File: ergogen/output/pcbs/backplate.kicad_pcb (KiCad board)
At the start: 2 copper layers, 124.2 x 110.1 mm, 5 parts

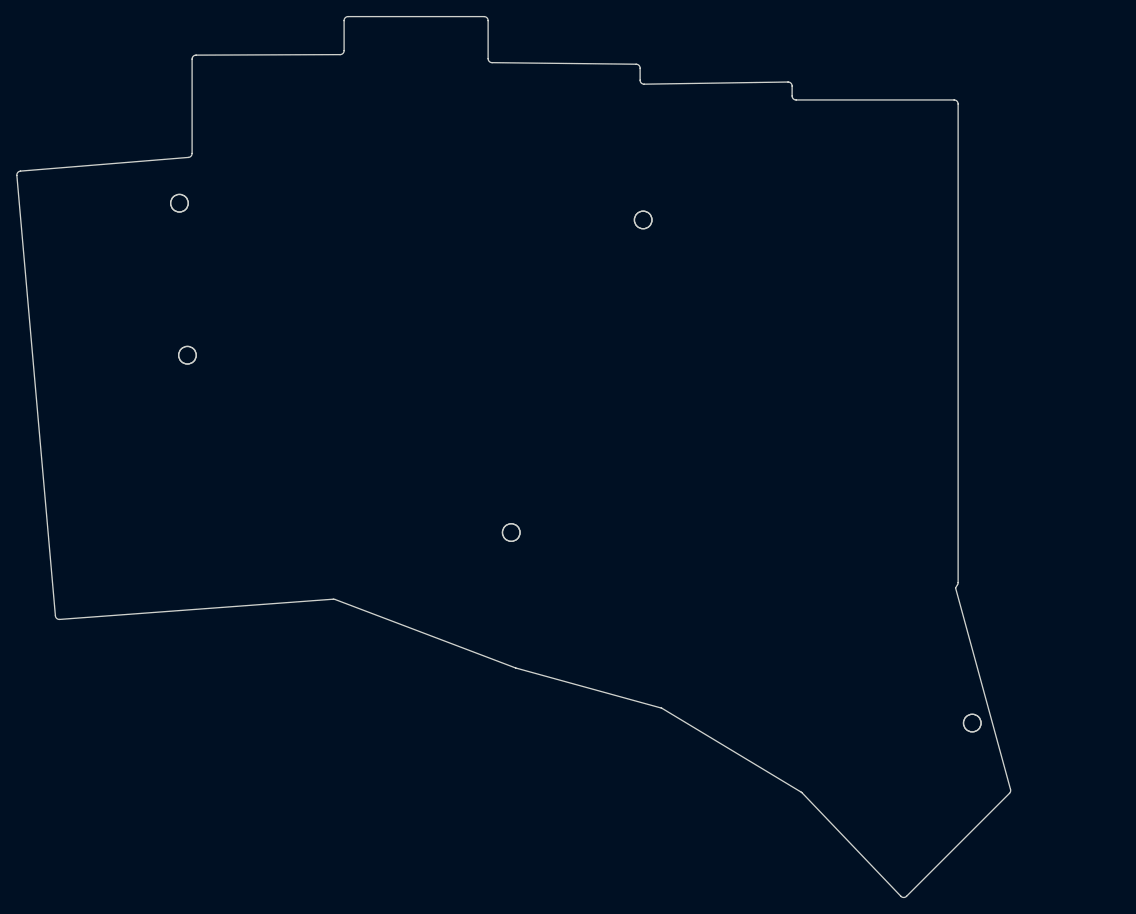
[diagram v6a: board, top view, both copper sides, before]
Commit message: Moved screws around a bit
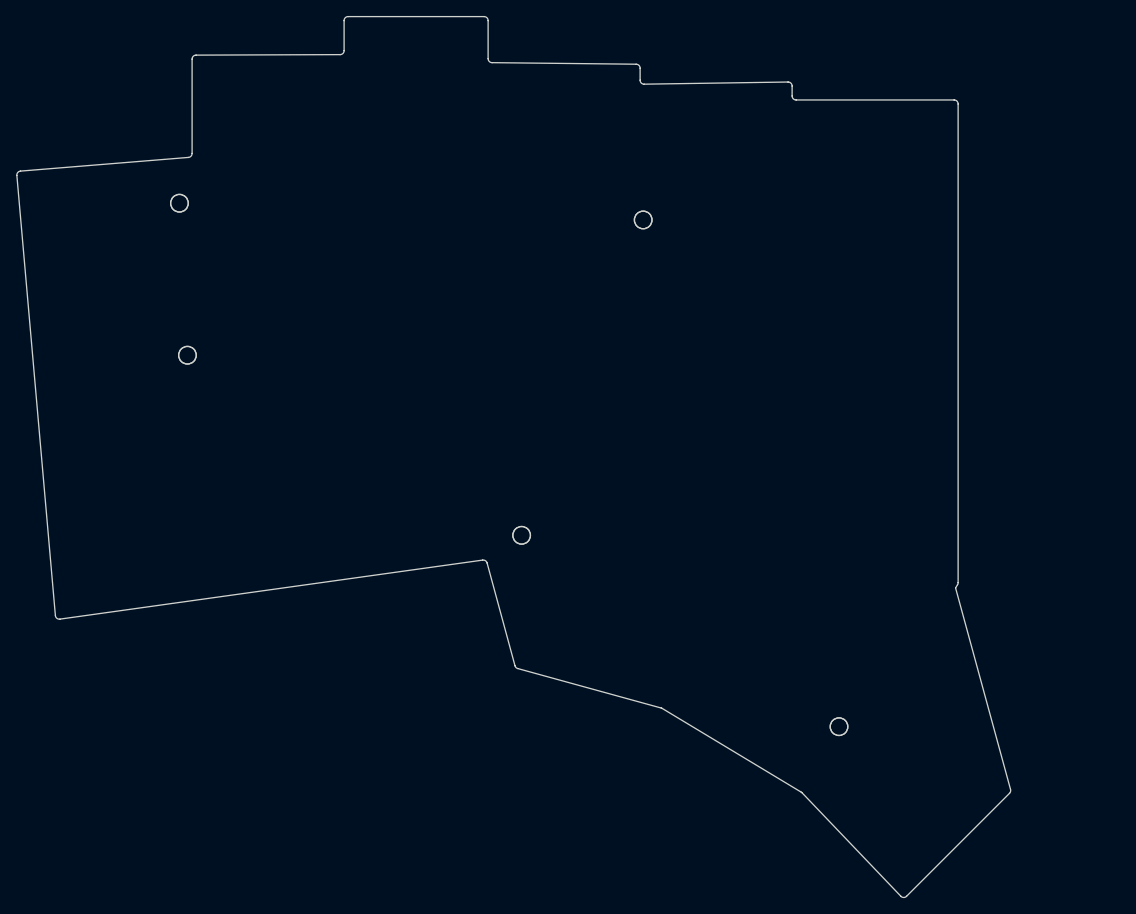
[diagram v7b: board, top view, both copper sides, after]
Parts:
- moved MH5 16.7 mm to (189.8, 123.4), turned to -30 degrees
- moved MH4 1.34 mm to (150.2, 99.4)
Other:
- outline, holes or cut-outs redrawn
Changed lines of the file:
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@@
   )
   (module "ceoloide:mounting_hole_npth" (layer F.Cu)
-      (at 148.8598077 99.0848776 -15)
+      (at 150.1570461 99.4324716 -15)
       (fp_text reference "MH4" (at 0 2.55 -15) (layer F.SilkS) hide (effects (font (size 1 1) (thickness 0.15))))
       (pad "" np_thru_hole circle (at 0 0 -15) (size 2.2 2.2) (drill 2.2) (layers *.Cu *.Mask))
   )
   (module "ceoloide:mounting_hole_npth" (layer F.Cu)
-      (at 206.488576 122.90275019999999 -45)
-      (fp_text reference "MH5" (at 0 2.55 -45) (layer F.SilkS) hide (effects (font (size 1 1) (thickness 0.15))))
-      (pad "" np_thru_hole circle (at 0 0 -45) (size 2.2 2.2) (drill 2.2) (layers *.Cu *.Mask))
+      (at 189.8298246 123.3510864 -30)
+      (fp_text reference "MH5" (at 0 2.55 -30) (layer F.SilkS) hide (effects (font (size 1 1) (thickness 0.15))))
+      (pad "" np_thru_hole circle (at 0 0 -30) (size 2.2 2.2) (drill 2.2) (layers *.Cu *.Mask))
   )
-  (gr_line (start 91.87824460323029 109.49068746980254) (end 87.06061104775414 54.447423555018986) (layer Edge.Cuts) (stroke (width 0.15) (type default)))
+  (gr_line (start 91.87535728883249 109.45769882370212) (end 87.06061104775414 54.447423555018986) (layer Edge.Cuts) (stroke (width 0.15) (type default)))
 (gr_line (start 87.51811429808367 53.90547845906503) (end 108.50503754967045 52.19601094528491) (layer Edge.Cuts) (stroke (width 0.15) (type default)))
 (gr_line (start 108.964445 51.69766144933076) (end 108.964445 39.90788282277217) (layer Edge.Cuts) (stroke (width 0.15) (type default)))
@@
 (gr_line (start 197.5573001306715 144.5456552181502) (end 185.2184018103768 131.6245719172887) (layer Edge.Cuts) (stroke (width 0.15) (type default)))
 (gr_line (start 185.11474537091743 131.54156036435938) (end 167.73632242747522 121.07577102297391) (layer Edge.Cuts) (stroke (width 0.15) (type default)))
-(gr_line (start 167.61101352447525 121.02201021014679) (end 149.42297909295323 116.01776895205687) (layer Edge.Cuts) (stroke (width 0.15) (type default)))
-(gr_line (start 149.37827902664569 116.003177061327) (end 126.82809141312292 107.44890800214452) (layer Edge.Cuts) (stroke (width 0.15) (type default)))
-(gr_line (start 126.61389341312291 107.4177619021445) (end 92.41319770323031 109.94573156980263) (layer Edge.Cuts) (stroke (width 0.15) (type default)))
+(gr_line (start 167.61101352447525 121.02201021014679) (end 149.67542832928424 116.0872276331902) (layer Edge.Cuts) (stroke (width 0.15) (type default)))
+(gr_line (start 149.32552987561743 115.73612318902917) (end 145.83984366392013 102.89472334271511) (layer Edge.Cuts) (stroke (width 0.15) (type default)))
+(gr_line (start 145.28816068340882 102.53050838832783) (end 92.4425969819845 109.90929922465821) (layer Edge.Cuts) (stroke (width 0.15) (type default)))
 (gr_line (start 184.46722317371226 45.01459040000001) (end 204.2174451 45.01459040000001) (layer Edge.Cuts) (stroke (width 0.15) (type default)))
 (gr_line (start 204.7174451 45.51459040000001) (end 204.7174451 105.34161580612954) (layer Edge.Cuts) (stroke (width 0.15) (type default)))
@@
 (gr_arc (start 185.21840173422504 131.62457194226215) (mid 185.16934173422504 131.57960944226215) (end 185.11474533422503 131.54156034226216) (layer Edge.Cuts) (stroke (width 0.15) (type default)))
 (gr_arc (start 167.7363223907828 121.07577100087666) (mid 167.6755091907828 121.04459890087666) (end 167.6110134907828 121.02201020087666) (layer Edge.Cuts) (stroke (width 0.15) (type default)))
-(gr_arc (start 149.37827902664569 116.003177061327) (mid 149.4004574266457 116.010998761327) (end 149.42297912664569 116.017768961327) (layer Edge.Cuts) (stroke (width 0.15) (type default)))
-(gr_arc (start 126.8280914131229 107.4489080021445) (mid 126.72269801312291 107.4216051021445) (end 126.61389341312291 107.4177619021445) (layer Edge.Cuts) (stroke (width 0.15) (type default)))
-(gr_arc (start 91.8782446032303 109.49068746980264) (mid 92.0523782032303 109.82794416980263) (end 92.4131977032303 109.94573156980263) (layer Edge.Cuts) (stroke (width 0.15) (type default)))
+(gr_arc (start 149.32552986297674 115.73612314246033) (mid 149.45390776297674 115.95808674246032) (end 149.67542826297674 116.08722764246032) (layer Edge.Cuts) (stroke (width 0.15) (type default)))
+(gr_arc (start 145.83984367656083 102.89472338928387) (mid 145.63278067656083 102.60843598928388) (end 145.28816067656084 102.53050828928387) (layer Edge.Cuts) (stroke (width 0.15) (type default)))
+(gr_arc (start 91.87535728883246 109.45769882370203) (mid 92.06202788883246 109.80527372370203) (end 92.44259698883246 109.90929922370204) (layer Edge.Cuts) (stroke (width 0.15) (type default)))
 (gr_circle (center 107.384445 57.919590400000004) (end 108.484445 57.919590400000004) (layer Edge.Cuts) (stroke (width 0.15) (type default)) (fill none))
 (gr_circle (center 108.384445 76.9195904) (end 109.484445 76.9195904) (layer Edge.Cuts) (stroke (width 0.15) (type default)) (fill none))
 (gr_circle (center 165.35244509999998 60.01059040000001) (end 166.45244509999998 60.01059040000001) (layer Edge.Cuts) (stroke (width 0.15) (type default)) (fill none))
-(gr_circle (center 148.8598077 99.0848776) (end 149.9598077 99.0848776) (layer Edge.Cuts) (stroke (width 0.15) (type default)) (fill none))
-(gr_circle (center 206.488576 122.90275019999999) (end 207.588576 122.90275019999999) (layer Edge.Cuts) (stroke (width 0.15) (type default)) (fill none))
+(gr_circle (center 150.1570461 99.4324716) (end 151.2570461 99.4324716) (layer Edge.Cuts) (stroke (width 0.15) (type default)) (fill none))
+(gr_circle (center 189.8298246 123.3510864) (end 190.9298246 123.3510864) (layer Edge.Cuts) (stroke (width 0.15) (type default)) (fill none))
 )

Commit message: Tweak shape
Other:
- board size 124.2 x 110.1 mm -> 124.1 x 110.1 mm
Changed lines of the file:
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@@
       (pad "" np_thru_hole circle (at 0 0 -30) (size 2.2 2.2) (drill 2.2) (layers *.Cu *.Mask))
   )
-  (gr_line (start 91.87535728883249 109.45769882370212) (end 87.06061104775414 54.447423555018986) (layer Edge.Cuts) (stroke (width 0.15) (type default)))
+  (gr_line (start 91.87827173174675 109.49099742324222) (end 87.06061104775414 54.447423555018986) (layer Edge.Cuts) (stroke (width 0.15) (type default)))
 (gr_line (start 87.51811429808367 53.90547845906503) (end 108.50503754967045 52.19601094528491) (layer Edge.Cuts) (stroke (width 0.15) (type default)))
 (gr_line (start 108.964445 51.69766144933076) (end 108.964445 39.90788282277217) (layer Edge.Cuts) (stroke (width 0.15) (type default)))
@@
 (gr_line (start 165.47394415076104 43.03997791277865) (end 183.45917122939375 42.77019950801905) (layer Edge.Cuts) (stroke (width 0.15) (type default)))
 (gr_line (start 183.96667038015485 43.26992130873259) (end 183.96722317371228 44.51481240004068) (layer Edge.Cuts) (stroke (width 0.15) (type default)))
-(gr_line (start 204.4024451 106.02118640000002) (end 211.26934923259245 131.2007277266382) (layer Edge.Cuts) (stroke (width 0.15) (type default)))
-(gr_line (start 211.1405195199005 131.68583548009948) (end 198.27245950682325 144.55389549317673) (layer Edge.Cuts) (stroke (width 0.15) (type default)))
+(gr_line (start 204.4024451 100.5601864) (end 185.55536086521693 99.2321005955616) (layer Edge.Cuts) (stroke (width 0.15) (type default)))
+(gr_line (start 185.13621331488523 100.05108698740453) (end 211.05315976360268 131.12986674538024) (layer Edge.Cuts) (stroke (width 0.15) (type default)))
+(gr_line (start 211.02271165951797 131.803643340482) (end 198.27245950682325 144.55389549317673) (layer Edge.Cuts) (stroke (width 0.15) (type default)))
 (gr_line (start 197.5573001306715 144.5456552181502) (end 185.2184018103768 131.6245719172887) (layer Edge.Cuts) (stroke (width 0.15) (type default)))
 (gr_line (start 185.11474537091743 131.54156036435938) (end 167.73632242747522 121.07577102297391) (layer Edge.Cuts) (stroke (width 0.15) (type default)))
-(gr_line (start 167.61101352447525 121.02201021014679) (end 149.67542832928424 116.0872276331902) (layer Edge.Cuts) (stroke (width 0.15) (type default)))
-(gr_line (start 149.32552987561743 115.73612318902917) (end 145.83984366392013 102.89472334271511) (layer Edge.Cuts) (stroke (width 0.15) (type default)))
-(gr_line (start 145.28816068340882 102.53050838832783) (end 92.4425969819845 109.90929922465821) (layer Edge.Cuts) (stroke (width 0.15) (type default)))
+(gr_line (start 167.61101352447525 121.02201021014679) (end 149.710817093128 116.09696446939239) (layer Edge.Cuts) (stroke (width 0.15) (type default)))
+(gr_line (start 149.3496706345805 115.69345582742767) (end 146.44949553337028 97.46837645346864) (layer Edge.Cuts) (stroke (width 0.15) (type default)))
+(gr_line (start 145.97070169267394 97.04717810078023) (end 108.98268763536329 95.93753767906091) (layer Edge.Cuts) (stroke (width 0.15) (type default)))
+(gr_line (start 108.4732258911544 96.51148092941446) (end 110.21182009800681 108.10245993570732) (layer Edge.Cuts) (stroke (width 0.15) (type default)))
+(gr_line (start 109.75389440169705 108.67529078487426) (end 92.41291032810221 109.9460646235092) (layer Edge.Cuts) (stroke (width 0.15) (type default)))
 (gr_line (start 184.46722317371226 45.01459040000001) (end 204.2174451 45.01459040000001) (layer Edge.Cuts) (stroke (width 0.15) (type default)))
-(gr_line (start 204.7174451 45.51459040000001) (end 204.7174451 105.34161580612954) (layer Edge.Cuts) (stroke (width 0.15) (type default)))
-(gr_line (start 204.65045780000003 105.59161580612948) (end 204.4024451 106.02118640000002) (layer Edge.Cuts) (stroke (width 0.15) (type default)))
+(gr_line (start 204.7174451 45.51459040000001) (end 204.7174451 99.88061580612953) (layer Edge.Cuts) (stroke (width 0.15) (type default)))
+(gr_line (start 204.65045780000003 100.13061580612947) (end 204.4024451 100.5601864) (layer Edge.Cuts) (stroke (width 0.15) (type default)))
 (gr_arc (start 87.51811424775414 53.90547845501909) (mid 87.17664344775413 54.0812949550191) (end 87.06061104775414 54.4474235550191) (layer Edge.Cuts) (stroke (width 0.15) (type default)))
 (gr_arc (start 108.5050376 52.19601094933076) (mid 108.83207 52.03655944933076) (end 108.964445 51.69766144933076) (layer Edge.Cuts) (stroke (width 0.15) (type default)))
@@
 (gr_arc (start 183.96722317371226 44.51481240003829) (mid 184.11374827371225 44.86822230003829) (end 184.46722317371226 45.01459040003829) (layer Edge.Cuts) (stroke (width 0.15) (type default)))
 (gr_arc (start 204.7174451 45.51459040000001) (mid 204.5709985 45.16103700000001) (end 204.2174451 45.01459040000001) (layer Edge.Cuts) (stroke (width 0.15) (type default)))
-(gr_arc (start 204.6504578 105.59161580612954) (mid 204.70040799999998 105.47102530612953) (end 204.7174451 105.34161580612954) (layer Edge.Cuts) (stroke (width 0.15) (type default)))
-(gr_arc (start 211.14051951990052 131.6858354800995) (mid 211.27021541990052 131.4606182800995) (end 211.2693492199005 131.2007276800995) (layer Edge.Cuts) (stroke (width 0.15) (type default)))
+(gr_arc (start 204.6504578 100.13061580612953) (mid 204.70040799999998 100.01002530612952) (end 204.7174451 99.88061580612953) (layer Edge.Cuts) (stroke (width 0.15) (type default)))
+(gr_arc (start 185.5553608189699 99.23210059230274) (mid 185.0751196189699 99.50306939230275) (end 185.1362134189699 100.05108699230274) (layer Edge.Cuts) (stroke (width 0.15) (type default)))
+(gr_arc (start 211.022711659518 131.80364334048204) (mid 211.16864855951798 131.47266194048203) (end 211.053159759518 131.12986674048204) (layer Edge.Cuts) (stroke (width 0.15) (type default)))
 (gr_arc (start 197.55730020682324 144.5456551931767) (mid 197.91314540682325 144.70030889317673) (end 198.27245950682325 144.5538953931767) (layer Edge.Cuts) (stroke (width 0.15) (type default)))
 (gr_arc (start 185.21840173422504 131.62457194226215) (mid 185.16934173422504 131.57960944226215) (end 185.11474533422503 131.54156034226216) (layer Edge.Cuts) (stroke (width 0.15) (type default)))
 (gr_arc (start 167.7363223907828 121.07577100087666) (mid 167.6755091907828 121.04459890087666) (end 167.6110134907828 121.02201020087666) (layer Edge.Cuts) (stroke (width 0.15) (type default)))
-(gr_arc (start 149.32552986297674 115.73612314246033) (mid 149.45390776297674 115.95808674246032) (end 149.67542826297674 116.08722764246032) (layer Edge.Cuts) (stroke (width 0.15) (type default)))
-(gr_arc (start 145.83984367656083 102.89472338928387) (mid 145.63278067656083 102.60843598928388) (end 145.28816067656084 102.53050828928387) (layer Edge.Cuts) (stroke (width 0.15) (type default)))
-(gr_arc (start 91.87535728883246 109.45769882370203) (mid 92.06202788883246 109.80527372370203) (end 92.44259698883246 109.90929922370204) (layer Edge.Cuts) (stroke (width 0.15) (type default)))
+(gr_arc (start 149.34967062682045 115.69345577866251) (mid 149.47088862682045 115.94833397866252) (end 149.71081702682045 116.09696447866251) (layer Edge.Cuts) (stroke (width 0.15) (type default)))
+(gr_arc (start 146.44949554113035 97.46837650223388) (mid 146.28596044113036 97.17154200223388) (end 145.97070174113034 97.04717810223387) (layer Edge.Cuts) (stroke (width 0.15) (type default)))
+(gr_arc (start 108.98268768381968 95.9375376805146) (mid 108.59376008381967 96.1053893805146) (end 108.47322578381967 96.5114808805146) (layer Edge.Cuts) (stroke (width 0.15) (type default)))
+(gr_arc (start 109.75389440534157 108.6752907846072) (mid 110.10789870534157 108.4888344846072) (end 110.21182010534156 108.1024599846072) (layer Edge.Cuts) (stroke (width 0.15) (type default)))
+(gr_arc (start 91.87827173174674 109.49099742324213) (mid 92.05228523174674 109.82815192324213) (end 92.41291033174674 109.94606462324214) (layer Edge.Cuts) (stroke (width 0.15) (type default)))
 (gr_circle (center 107.384445 57.919590400000004) (end 108.484445 57.919590400000004) (layer Edge.Cuts) (stroke (width 0.15) (type default)) (fill none))
 (gr_circle (center 108.384445 76.9195904) (end 109.484445 76.9195904) (layer Edge.Cuts) (stroke (width 0.15) (type default)) (fill none))
